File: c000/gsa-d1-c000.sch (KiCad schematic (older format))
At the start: 27 parts, among them J301 CONN-4, J302 CONN-3, J303 CONN-3, J304 CONN-3, J305 CONN-3, J306 CONN-3, J307 CONN-2, J308 CONN-3, U301 4066, U302 4066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

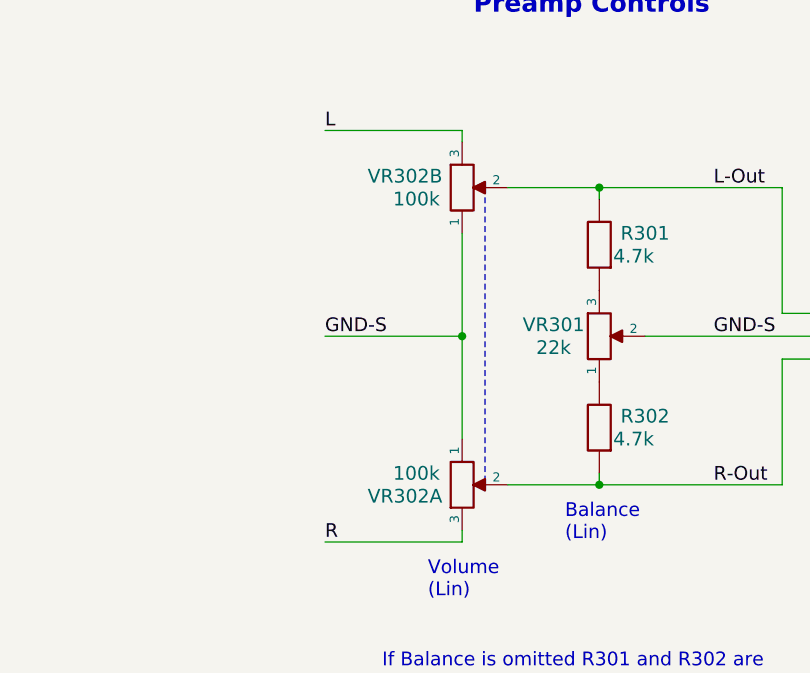
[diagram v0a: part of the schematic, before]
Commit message: Minor layout improvements to pre-amp controls
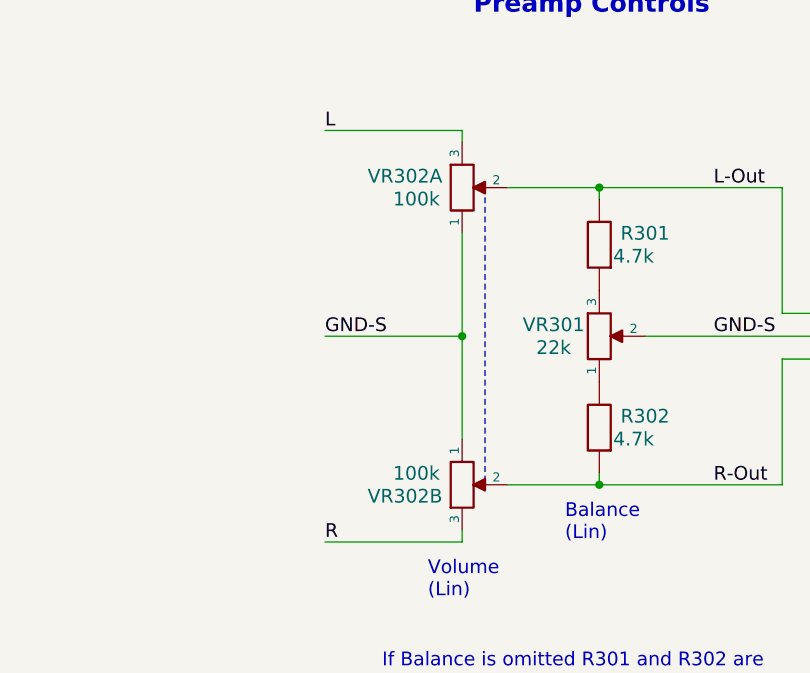
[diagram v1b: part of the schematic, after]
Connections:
- net GND-S: now also VR302.1, VR302.4 (1); no longer VR302.1, VR302.4 (1)
- net L: now also VR302.6 (3); no longer VR302.3
- net L-Out: now also VR302.5 (2); no longer VR302.2
- net R: now also VR302.3; no longer VR302.6 (3)
- net R-Out: now also VR302.2; no longer VR302.5 (2)
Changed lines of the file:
@@
 EESchema Schematic File Version 2
 LIBS:gsa
+LIBS:gsa-d1-c000-cache
 EELAYER 25 0
 EELAYER END
 $Descr A4 11693 8268
 encoding utf-8
-Sheet 3 5
+Sheet 1 1
 Title "Diamond-1"
 Date "January 2018"
-Rev "2.0.0"
+Rev "2.0.1"
 Comp "Gemstone Amplification"
 Comment1 "© Tim Baldwin 2016,2018"
-Comment2 "GSA-D1-C200"
+Comment2 "GSA-D1-C201"
 Comment3 "Pre-Amp Controls and Input Switching"
 Comment4 "Stereo Amplifier"
@@
 $Comp
 L POT-D VR302
-U 2 1 5A85ECFC
+U 1 1 5A85ECFC
 P 7950 2050
 F 0 "VR302" H 7700 2100 60  0000 C CNN
@@
 F 2 "gsa:POT-DUAL" H 7950 2050 60  0001 C CNN
 F 3 "" H 7950 2050 60  0000 C CNN
-	2    7950 2050
+	1    7950 2050
 	1    0    0    -1
 $EndComp
 $Comp
 L POT-D VR302
-U 1 1 5A85ECFD
+U 2 1 5A85ECFD
 P 7950 3350
 F 0 "VR302" H 7700 3400 60  0000 C CNN
@@
 F 2 "gsa:POT-DUAL" H 7950 3350 60  0001 C CNN
 F 3 "" H 7950 3350 60  0000 C CNN
-	1    7950 3350
+	2    7950 3350
 	1    0    0    1
 $EndComp

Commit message: Updated to use KiCad v5
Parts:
- C301, C304, C305: symbol CAP -> gsa:CAP
- C302, C303: symbol CAP-P -> gsa:CAP-P
- D301, D302: symbol DIODE -> gsa:DIODE
- H301, H302: symbol HOLE -> gsa:HOLE
- J301: symbol CONN-4 -> gsa:CONN-4
- J302, J303, J304, J305, J306, J308: symbol CONN-3 -> gsa:CONN-3
- J307: symbol CONN-2 -> gsa:CONN-2
- R301, R302: symbol RES -> gsa:RES
- U301, U302: symbol 4066 -> gsa:4066
- U303: symbol LM79XX -> gsa:LM79XX
- U304: symbol LM78XX -> gsa:LM78XX
- VR301: symbol POT -> gsa:POT
- VR302: symbol POT-D -> gsa:POT-D
- X301, X302: symbol LINK -> gsa:LINK
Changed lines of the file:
@@
-EESchema Schematic File Version 2
+EESchema Schematic File Version 4
 LIBS:gsa
 LIBS:gsa-d1-cache
-EELAYER 25 0
+EELAYER 29 0
 EELAYER END
 $Descr A4 11693 8268
@@
 Sheet 3 5
 Title "Diamond-1"
-Date "January 2018"
+Date "May 2019"
 Rev "2.0.1"
 Comp "Gemstone Amplification"
-Comment1 "© Tim Baldwin 2016,2018"
+Comment1 "© Tim Baldwin 2016,2019"
 Comment2 "GSA-D1-C201"
 Comment3 "Pre-Amp Controls and Input Switching"
@@
 $EndDescr
 $Comp
-L 4066 U301
+L gsa:4066 U301
 U 1 1 5A85ECF9
 P 3250 2200
@@
 $EndComp
 $Comp
-L CAP C301
+L gsa:CAP C301
 U 1 1 5A85ECFA
 P 2600 2700
@@
 $EndComp
 $Comp
-L 4066 U302
+L gsa:4066 U302
 U 1 1 5A85ECFB
 P 3250 3200
@@
 D
 $Comp
-L POT-D VR302
+L gsa:POT-D VR302
 U 1 1 5A85ECFC
 P 7950 2050
@@
 $EndComp
 $Comp
-L POT-D VR302
+L gsa:POT-D VR302
 U 2 1 5A85ECFD
 P 7950 3350
@@
 Balance\n(Lin)
 $Comp
-L CONN-2 J307
+L gsa:CONN-2 J307
 U 1 1 5A85ECFF
 P 5400 6000
@@
 $EndComp
 $Comp
-L HOLE H301
+L gsa:HOLE H301
 U 1 1 5A85ED00
 P 1450 4550
@@
 $EndComp
 $Comp
-L HOLE H302
+L gsa:HOLE H302
 U 1 1 5A85ED01
 P 1950 4550
@@
 R
 $Comp
-L CONN-3 J302
+L gsa:CONN-3 J302
 U 1 1 5A85ED02
 P 2050 6050
@@
 V-
 $Comp
-L LM78XX U304
+L gsa:LM78XX U304
 U 1 1 5A85ED03
 P 3650 5400
@@
 $EndComp
 $Comp
-L LM79XX U303
+L gsa:LM79XX U303
 U 1 1 5A85ED04
 P 3650 6700
@@
 $EndComp
 $Comp
-L CAP-P C302
+L gsa:CAP-P C302
 U 1 1 5A85ED05
 P 3150 5750
@@
 $EndComp
 $Comp
-L CAP-P C303
+L gsa:CAP-P C303
 U 1 1 5A85ED06
 P 3150 6350
@@
 $EndComp
 $Comp
-L CAP C304
+L gsa:CAP C304
 U 1 1 5A85ED07
 P 4150 5750
@@
 $EndComp
 $Comp
-L CAP C305
+L gsa:CAP C305
 U 1 1 5A85ED08
 P 4150 6350
@@
 $EndComp
 $Comp
-L DIODE D301
+L gsa:DIODE D301
 U 1 1 5A85ED09
 P 4550 5750
@@
 $EndComp
 $Comp
-L DIODE D302
+L gsa:DIODE D302
 U 1 1 5A85ED0A
 P 4550 6350
@@
 $EndComp
 $Comp
-L CONN-4 J301
+L gsa:CONN-4 J301
 U 1 1 5A85ED0B
 P 1500 2650
@@
 Vin-
 $Comp
-L LINK X301
+L gsa:LINK X301
 U 1 1 5A85ED0C
 P 3950 2550
@@
 $EndComp
 $Comp
-L LINK X302
+L gsa:LINK X302
 U 1 1 5A85ED0D
 P 3950 2750
@@
 	3500 2000 3750 2000
 Wire Wire Line
-	3750 1750 3750 3150
+	3750 1750 3750 2000
 Wire Wire Line
 	3750 2150 3500 2150
@@
 	3600 2450 3500 2450
 Wire Wire Line
-	3600 2300 3600 3650
+	3600 2300 3600 2450
 Connection ~ 3600 2450
 Wire Wire Line
@@
 	4150 1750 5050 1750
 Wire Wire Line
-	4150 1750 4150 2550
+	4150 1750 4150 2100
 Wire Wire Line
 	4150 2100 3500 2100
@@
 	4550 2250 4550 2050
 Wire Wire Line
-	3500 2250 4550 2250
+	3500 2250 4250 2250
 Wire Wire Line
 	4150 2850 5050 2850
@@
 	2250 2550 2250 2150
 Wire Wire Line
-	2250 2150 3000 2150
+	2250 2150 2900 2150
 Wire Wire Line
 	3000 2250 2900 2250
@@
 	2350 2650 2350 2300
 Wire Wire Line
-	2350 2300 3000 2300
+	2350 2300 2800 2300
 Wire Wire Line
 	2800 2100 2800 2300
@@
 	2350 2750 2350 3150
 Wire Wire Line
-	2350 3150 3000 3150
+	2350 3150 2900 3150
 Wire Wire Line
 	3000 3250 2900 3250
@@
 	2250 2850 2250 3300
 Wire Wire Line
-	2250 3300 3000 3300
+	2250 3300 2800 3300
 Wire Wire Line
 	3000 3100 2800 3100
@@
 Connection ~ 2800 3300
 Wire Wire Line
-	2400 5400 3300 5400
-Wire Wire Line
-	2400 6700 3300 6700
+	2400 5400 3150 5400
+Wire Wire Line
+	2400 6700 3150 6700
 Wire Wire Line
 	5100 5400 5100 6000
@@
 	2400 6150 2400 6700
 Wire Wire Line
-	2600 1650 2600 2550
-Wire Wire Line
-	2250 6050 4550 6050
-Wire Wire Line
-	3650 5650 3650 6450
+	2600 1650 2600 2450
+Wire Wire Line
+	2250 6050 3150 6050
+Wire Wire Line
+	3650 5650 3650 6050
 Connection ~ 3650 6050
 Wire Wire Line
-	4000 5400 5300 5400
-Wire Wire Line
-	4000 6700 5300 6700
+	4000 5400 4150 5400
+Wire Wire Line
+	4000 6700 4150 6700
 Wire Wire Line
 	3150 5600 3150 5400
 Connection ~ 3150 5400
 Wire Wire Line
-	3150 5900 3150 6200
+	3150 5900 3150 6050
 Connection ~ 3150 6050
 Wire Wire Line
@@
 Connection ~ 4150 5400
 Wire Wire Line
-	4150 5900 4150 6200
+	4150 5900 4150 6050
 Connection ~ 4150 6050
 Wire Wire Line
-	4550 5900 4550 6150
+	4550 5900 4550 6050
 Connection ~ 4550 6050
 Wire Wire Line
@@
 Connection ~ 5100 6700
 Wire Wire Line
-	3100 1850 3100 1850
-Wire Wire Line
-	2400 1650 3100 1650
+	2400 1650 2600 1650
 Wire Wire Line
 	3100 3750 3100 3550
 Wire Wire Line
-	2600 2850 2600 3750
-Wire Wire Line
-	2400 3750 3100 3750
+	2600 2850 2600 2950
+Wire Wire Line
+	2400 3750 2600 3750
 Connection ~ 2600 1650
 Connection ~ 2600 3750
@@
 Connection ~ 4250 2250
 $Comp
-L CONN-3 J308
+L gsa:CONN-3 J308
 U 1 1 5A85ED0E
 P 9700 2700
@@
 	4550 2500 5050 2500
 $Comp
-L CONN-3 J306
+L gsa:CONN-3 J306
 U 1 1 5A85ED0F
 P 5250 1850
@@
 $EndComp
 $Comp
-L CONN-3 J305
+L gsa:CONN-3 J305
 U 1 1 5A85ED10
 P 5250 2400
@@
 $EndComp
 $Comp
-L CONN-3 J304
+L gsa:CONN-3 J304
 U 1 1 5A85ED11
 P 5250 2950
@@
 $EndComp
 $Comp
-L CONN-3 J303
+L gsa:CONN-3 J303
 U 1 1 5A85ED12
 P 5250 3500
@@
 	5050 1850 5000 1850
 Wire Wire Line
-	5000 1850 5000 3850
+	5000 1850 5000 2400
 Wire Wire Line
 	5000 2400 5050 2400
@@
 	7350 1800 7950 1800
 $Comp
-L POT VR301
+L gsa:POT VR301
 U 1 1 5A85ECFE
 P 8550 2700
@@
 If Balance is omitted R301 and R302 are\nrequired, should be 10k-15k and \nshould be connected to GND-S.
 $Comp
-L RES R301
+L gsa:RES R301
 U 1 1 5A8B4D38
 P 8550 2300
@@
 $EndComp
 $Comp
-L RES R302
+L gsa:RES R302
 U 1 1 5A8B4FE5
 P 8550 3100
@@
 $EndComp
 Wire Wire Line
-	7950 2250 7950 3150
+	7950 2250 7950 2700
 Wire Wire Line
 	7950 1800 7950 1850
@@
 Connection ~ 7950 2700
 Wire Wire Line
-	8150 3350 9350 3350
+	8150 3350 8550 3350
 Wire Wire Line
 	9350 3350 9350 2800
@@
 	9350 2050 9350 2600
 Wire Wire Line
-	8150 2050 9350 2050
+	8150 2050 8550 2050
 Wire Wire Line
 	8750 2700 9500 2700
@@
 Wire Wire Line
 	4750 1950 5050 1950
+Wire Wire Line
+	3750 2150 3750 2550
+Wire Wire Line
+	3750 3000 3750 3150
+Wire Wire Line
+	3600 2450 3600 2750
+Wire Wire Line
+	3600 3300 3600 3450
+Wire Wire Line
+	2900 2150 3000 2150
+Wire Wire Line
+	2800 2300 3000 2300
+Wire Wire Line
+	2900 3150 3000 3150
+Wire Wire Line
+	2800 3300 3000 3300
+Wire Wire Line
+	3650 6050 4150 6050
+Wire Wire Line
+	3650 6050 3650 6450
+Wire Wire Line
+	3150 5400 3300 5400
+Wire Wire Line
+	3150 6050 3650 6050
+Wire Wire Line
+	3150 6050 3150 6200
+Wire Wire Line
+	3150 6700 3300 6700
+Wire Wire Line
+	4150 6700 4550 6700
+Wire Wire Line
+	4150 5400 4550 5400
+Wire Wire Line
+	4150 6050 4150 6200
+Wire Wire Line
+	4150 6050 4550 6050
+Wire Wire Line
+	4550 6050 4550 6150
+Wire Wire Line
+	4550 5400 5100 5400
+Wire Wire Line
+	4550 6700 5100 6700
+Wire Wire Line
+	5100 5400 5300 5400
+Wire Wire Line
+	5100 6700 5300 6700
+Wire Wire Line
+	2600 1650 3100 1650
+Wire Wire Line
+	2600 3750 3100 3750
+Wire Wire Line
+	2600 2950 2600 3750
+Wire Wire Line
+	2600 2450 2600 2550
+Wire Wire Line
+	3750 2000 3750 2150
+Wire Wire Line
+	3600 2750 3600 3300
+Wire Wire Line
+	3750 2550 3750 3000
+Wire Wire Line
+	4150 2100 4150 2550
+Wire Wire Line
+	4250 2250 4550 2250
+Wire Wire Line
+	5000 2400 5000 2950
+Wire Wire Line
+	5000 2950 5000 3500
+Wire Wire Line
+	5000 3500 5000 3850
+Wire Wire Line
+	7950 2700 7950 3150
+Wire Wire Line
+	8550 2050 9350 2050
+Wire Wire Line
+	8550 3350 9350 3350
+Wire Wire Line
+	3600 3450 3600 3650
 $EndSCHEMATC
